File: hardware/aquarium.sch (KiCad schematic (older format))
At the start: 3 parts, among them J1 Arduino Nano, U1 DS18B20

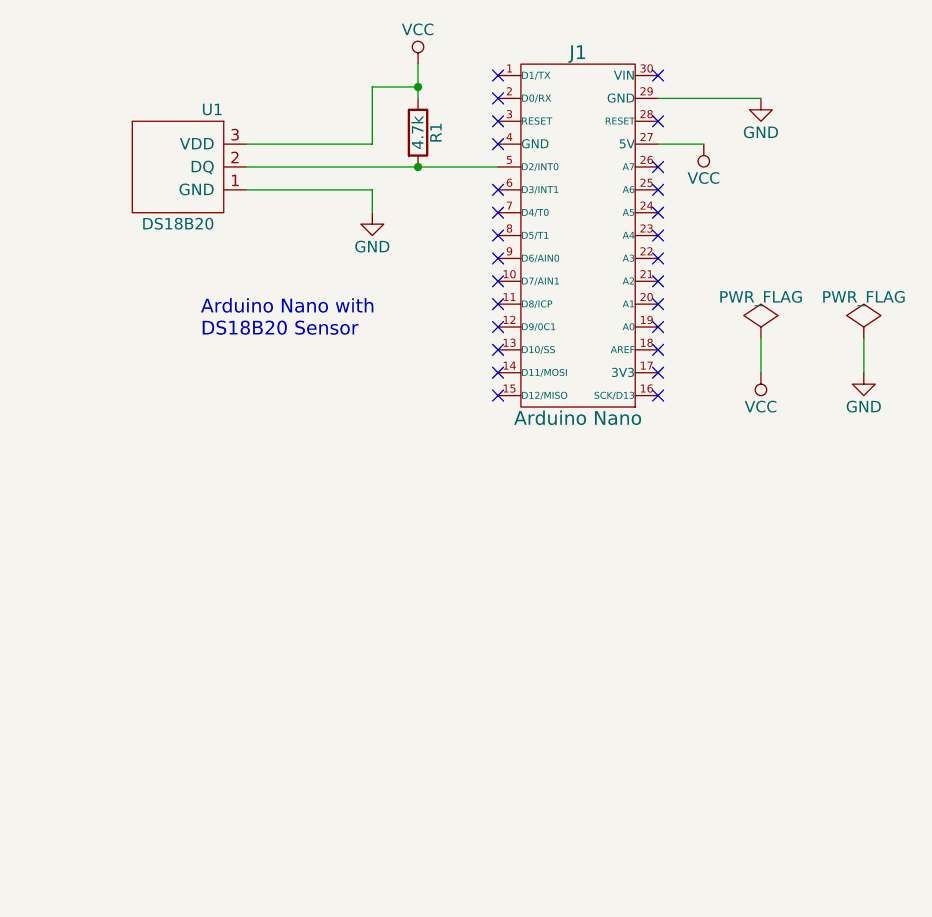
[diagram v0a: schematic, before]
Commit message: changed hardare, added rotary encoder code
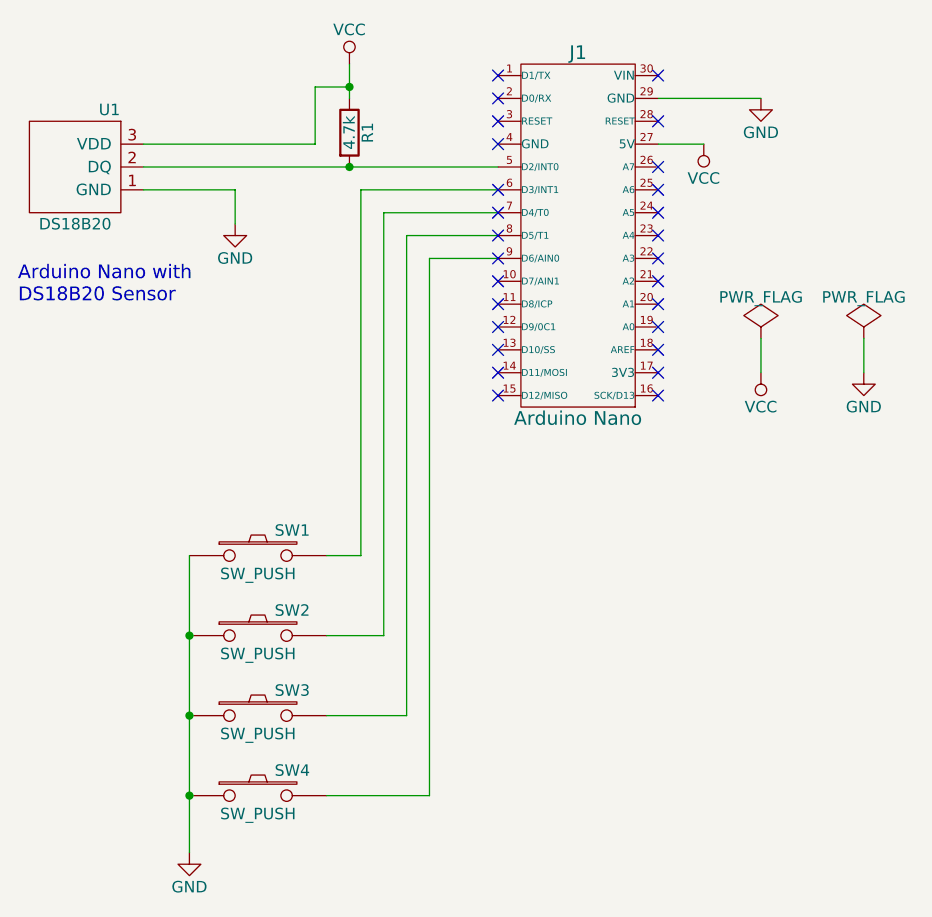
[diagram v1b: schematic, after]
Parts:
- added SW1, SW2, SW3, SW4: SW_PUSH, symbol SW_PUSH
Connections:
- net GND: now also SW1.1, SW2.1, SW3.1, SW4.1
- net at J1.6 (D3/INT1): now also SW1.2
- net at J1.7 (D4/T0): now also SW2.2
- net at J1.8 (D5/T1): now also SW3.2
- net at J1.9 (D6/AIN0): now also SW4.2
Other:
- moved on the sheet: R1, U1
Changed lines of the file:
@@
 LIBS:w_connectors
 LIBS:maxim
+LIBS:aquarium-cache
 EELAYER 25 0
 EELAYER END
@@
 L DS18B20 U1
 U 1 1 56BB9483
-P 2250 2450
-F 0 "U1" H 2100 2700 50  0000 C CNN
-F 1 "DS18B20" H 2250 2200 50  0000 C CNN
-F 2 "TO_SOT_Packages_THT:TO-92_Inline_Narrow_Oval" H 2100 2700 50  0001 C CNN
-F 3 "" H 2100 2700 50  0000 C CNN
-	1    2250 2450
+P 1800 2450
+F 0 "U1" H 1650 2700 50  0000 C CNN
+F 1 "DS18B20" H 1800 2200 50  0000 C CNN
+F 2 "TO_SOT_Packages_THT:TO-92_Inline_Narrow_Oval" H 1650 2700 50  0001 C CNN
+F 3 "" H 1650 2700 50  0000 C CNN
+	1    1800 2450
 	-1   0    0    -1
 $EndComp
@@
 L R R1
 U 1 1 56BB952E
-P 3300 2300
-F 0 "R1" V 3380 2300 50  0000 C CNN
-F 1 "4.7k" V 3300 2300 50  0000 C CNN
-F 2 "Resistors_ThroughHole:Resistor_Horizontal_RM7mm" V 3230 2300 50  0001 C CNN
-F 3 "" H 3300 2300 50  0000 C CNN
-	1    3300 2300
-	1    0    0    -1
-$EndComp
-$Comp
-L GND #PWR01
+P 3000 2300
+F 0 "R1" V 3080 2300 50  0000 C CNN
+F 1 "4.7k" V 3000 2300 50  0000 C CNN
+F 2 "Resistors_ThroughHole:Resistor_Horizontal_RM7mm" V 2930 2300 50  0001 C CNN
+F 3 "" H 3000 2300 50  0000 C CNN
+	1    3000 2300
+	1    0    0    -1
+$EndComp
+$Comp
+L GND #PWR5
 U 1 1 56BB965D
 P 4800 2150
-F 0 "#PWR01" H 4800 1900 50  0001 C CNN
+F 0 "#PWR5" H 4800 1900 50  0001 C CNN
 F 1 "GND" H 4800 2000 50  0000 C CNN
 F 2 "" H 4800 2150 50  0000 C CNN
@@
 $EndComp
 $Comp
-L GND #PWR02
+L GND #PWR2
 U 1 1 56BB9677
-P 3100 2650
-F 0 "#PWR02" H 3100 2400 50  0001 C CNN
-F 1 "GND" H 3100 2500 50  0000 C CNN
-F 2 "" H 3100 2650 50  0000 C CNN
-F 3 "" H 3100 2650 50  0000 C CNN
-	1    3100 2650
-	1    0    0    -1
-$EndComp
-$Comp
-L VCC #PWR03
+P 2500 2700
+F 0 "#PWR2" H 2500 2450 50  0001 C CNN
+F 1 "GND" H 2500 2550 50  0000 C CNN
+F 2 "" H 2500 2700 50  0000 C CNN
+F 3 "" H 2500 2700 50  0000 C CNN
+	1    2500 2700
+	1    0    0    -1
+$EndComp
+$Comp
+L VCC #PWR4
 U 1 1 56BB9691
 P 4550 2350
-F 0 "#PWR03" H 4550 2200 50  0001 C CNN
+F 0 "#PWR4" H 4550 2200 50  0001 C CNN
 F 1 "VCC" H 4550 2500 50  0000 C CNN
 F 2 "" H 4550 2350 50  0000 C CNN
@@
 $EndComp
 $Comp
-L VCC #PWR04
+L VCC #PWR3
 U 1 1 56BB96D2
-P 3300 2000
-F 0 "#PWR04" H 3300 1850 50  0001 C CNN
-F 1 "VCC" H 3300 2150 50  0000 C CNN
-F 2 "" H 3300 2000 50  0000 C CNN
-F 3 "" H 3300 2000 50  0000 C CNN
-	1    3300 2000
+P 3000 2000
+F 0 "#PWR3" H 3000 1850 50  0001 C CNN
+F 1 "VCC" H 3000 2150 50  0000 C CNN
+F 2 "" H 3000 2000 50  0000 C CNN
+F 3 "" H 3000 2000 50  0000 C CNN
+	1    3000 2000
 	1    0    0    -1
 $EndComp
@@
 	4350 2150 4800 2150
 Wire Wire Line
-	2550 2550 3100 2550
-Wire Wire Line
-	3100 2550 3100 2650
-Wire Wire Line
-	2550 2450 3650 2450
-Connection ~ 3300 2450
-Wire Wire Line
-	3300 2000 3300 2150
+	2100 2550 2500 2550
+Wire Wire Line
+	2500 2550 2500 2700
+Wire Wire Line
+	2100 2450 3650 2450
+Connection ~ 3000 2450
+Wire Wire Line
+	3000 2000 3000 2150
 NoConn ~ 4350 2050
 NoConn ~ 4350 2250
@@
 NoConn ~ 3650 2050
 $Comp
-L PWR_FLAG #FLG05
+L PWR_FLAG #FLG1
 U 1 1 56BB9BB9
 P 4800 3200
-F 0 "#FLG05" H 4800 3295 50  0001 C CNN
+F 0 "#FLG1" H 4800 3295 50  0001 C CNN
 F 1 "PWR_FLAG" H 4800 3380 50  0000 C CNN
 F 2 "" H 4800 3200 50  0000 C CNN
@@
 $EndComp
 $Comp
-L PWR_FLAG #FLG06
+L PWR_FLAG #FLG2
 U 1 1 56BB9BD3
 P 5250 3200
-F 0 "#FLG06" H 5250 3295 50  0001 C CNN
+F 0 "#FLG2" H 5250 3295 50  0001 C CNN
 F 1 "PWR_FLAG" H 5250 3380 50  0000 C CNN
 F 2 "" H 5250 3200 50  0000 C CNN
@@
 $EndComp
 $Comp
-L GND #PWR07
+L GND #PWR7
 U 1 1 56BB9BED
 P 5250 3350
-F 0 "#PWR07" H 5250 3100 50  0001 C CNN
+F 0 "#PWR7" H 5250 3100 50  0001 C CNN
 F 1 "GND" H 5250 3200 50  0000 C CNN
 F 2 "" H 5250 3350 50  0000 C CNN
@@
 $EndComp
 $Comp
-L VCC #PWR08
+L VCC #PWR6
 U 1 1 56BB9C0A
 P 4800 3350
-F 0 "#PWR08" H 4800 3200 50  0001 C CNN
+F 0 "#PWR6" H 4800 3200 50  0001 C CNN
 F 1 "VCC" H 4800 3500 50  0000 C CNN
 F 2 "" H 4800 3350 50  0000 C CNN
@@
 	5250 3200 5250 3350
 Wire Wire Line
-	2550 2350 3100 2350
-Wire Wire Line
-	3100 2350 3100 2100
-Wire Wire Line
-	3100 2100 3300 2100
-Connection ~ 3300 2100
-Text Notes 2350 3200 0    60   ~ 0
+	2100 2350 2850 2350
+Wire Wire Line
+	2850 2350 2850 2100
+Wire Wire Line
+	2850 2100 3000 2100
+Connection ~ 3000 2100
+Text Notes 1550 3050 0    60   ~ 0
 Arduino Nano with \nDS18B20 Sensor
+$Comp
+L SW_PUSH SW2
+U 1 1 56C9D178
+P 2600 4500
+F 0 "SW2" H 2750 4610 50  0000 C CNN
+F 1 "SW_PUSH" H 2600 4420 50  0000 C CNN
+F 2 "" H 2600 4500 50  0000 C CNN
+F 3 "" H 2600 4500 50  0000 C CNN
+	1    2600 4500
+	1    0    0    -1
+$EndComp
+$Comp
+L SW_PUSH SW3
+U 1 1 56C9D223
+P 2600 4850
+F 0 "SW3" H 2750 4960 50  0000 C CNN
+F 1 "SW_PUSH" H 2600 4770 50  0000 C CNN
+F 2 "" H 2600 4850 50  0000 C CNN
+F 3 "" H 2600 4850 50  0000 C CNN
+	1    2600 4850
+	1    0    0    -1
+$EndComp
+$Comp
+L SW_PUSH SW1
+U 1 1 56C9D2EA
+P 2600 4150
+F 0 "SW1" H 2750 4260 50  0000 C CNN
+F 1 "SW_PUSH" H 2600 4070 50  0000 C CNN
+F 2 "" H 2600 4150 50  0000 C CNN
+F 3 "" H 2600 4150 50  0000 C CNN
+	1    2600 4150
+	1    0    0    -1
+$EndComp
+$Comp
+L SW_PUSH SW4
+U 1 1 56C9D313
+P 2600 5200
+F 0 "SW4" H 2750 5310 50  0000 C CNN
+F 1 "SW_PUSH" H 2600 5120 50  0000 C CNN
+F 2 "" H 2600 5200 50  0000 C CNN
+F 3 "" H 2600 5200 50  0000 C CNN
+	1    2600 5200
+	1    0    0    -1
+$EndComp
+Wire Wire Line
+	3650 2550 3050 2550
+Wire Wire Line
+	3050 2550 3050 4150
+Wire Wire Line
+	3050 4150 2900 4150
+Wire Wire Line
+	3650 2650 3150 2650
+Wire Wire Line
+	3150 2650 3150 4500
+Wire Wire Line
+	3150 4500 2900 4500
+Wire Wire Line
+	3650 2750 3250 2750
+Wire Wire Line
+	3250 2750 3250 4850
+Wire Wire Line
+	3250 4850 2900 4850
+Wire Wire Line
+	3650 2850 3350 2850
+Wire Wire Line
+	3350 2850 3350 5200
+Wire Wire Line
+	3350 5200 2900 5200
+Wire Wire Line
+	2300 4150 2300 5450
+Connection ~ 2300 4500
+Connection ~ 2300 4850
+$Comp
+L GND #PWR1
+U 1 1 56C9D9F6
+P 2300 5450
+F 0 "#PWR1" H 2300 5200 50  0001 C CNN
+F 1 "GND" H 2300 5300 50  0000 C CNN
+F 2 "" H 2300 5450 50  0000 C CNN
+F 3 "" H 2300 5450 50  0000 C CNN
+	1    2300 5450
+	1    0    0    -1
+$EndComp
+Connection ~ 2300 5200
 $EndSCHEMATC
